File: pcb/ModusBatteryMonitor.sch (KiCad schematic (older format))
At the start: 17 parts, among them IC101 ATTINY3224-SS, IC102 MAX485/3485, P101 RS485, P102 NTC1, P103 NTC2, P104 DEBUG, P105 SHUNT+, P106 SHUNT-, P107 BAT-, U101 NCP1117ST50T3G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

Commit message: Made housing
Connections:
- net RS485-A: now also IC102.6 (A); no longer IC102.7 (B)
- net RS485-B: now also IC102.7 (B); no longer IC102.6 (A)
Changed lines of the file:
@@
 	1    0    0    -1
 $EndComp
+Text GLabel 9700 3650 2    60   BiDi ~ 0
+RS485-A
 Text GLabel 9700 3450 2    60   BiDi ~ 0
-RS485-A
-Text GLabel 9700 3650 2    60   BiDi ~ 0
 RS485-B
 $Comp

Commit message: Fixed NtC sensors and adjusted LUT
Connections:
- net RS485-A: now also P101.4; no longer P101.3
- net RS485-B: now also P101.3; no longer P101.4
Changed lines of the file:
@@
 	1    0    0    -1
 $EndComp
+Text GLabel 9500 4550 0    60   BiDi ~ 0
+RS485-A
 Text GLabel 9500 4450 0    60   BiDi ~ 0
-RS485-A
-Text GLabel 9500 4550 0    60   BiDi ~ 0
 RS485-B
 Text GLabel 9500 4350 0    60   BiDi ~ 0
@@
 	8500 5200 8500 5250
 $Comp
-L GND #PWR?
+L GND #PWR011
 U 1 1 63A05406
 P 9500 4650
-F 0 "#PWR?" H 9500 4650 30  0001 C CNN
+F 0 "#PWR011" H 9500 4650 30  0001 C CNN
 F 1 "GND" H 9500 4580 30  0001 C CNN
 F 2 "" H 9500 4650 60  0001 C CNN

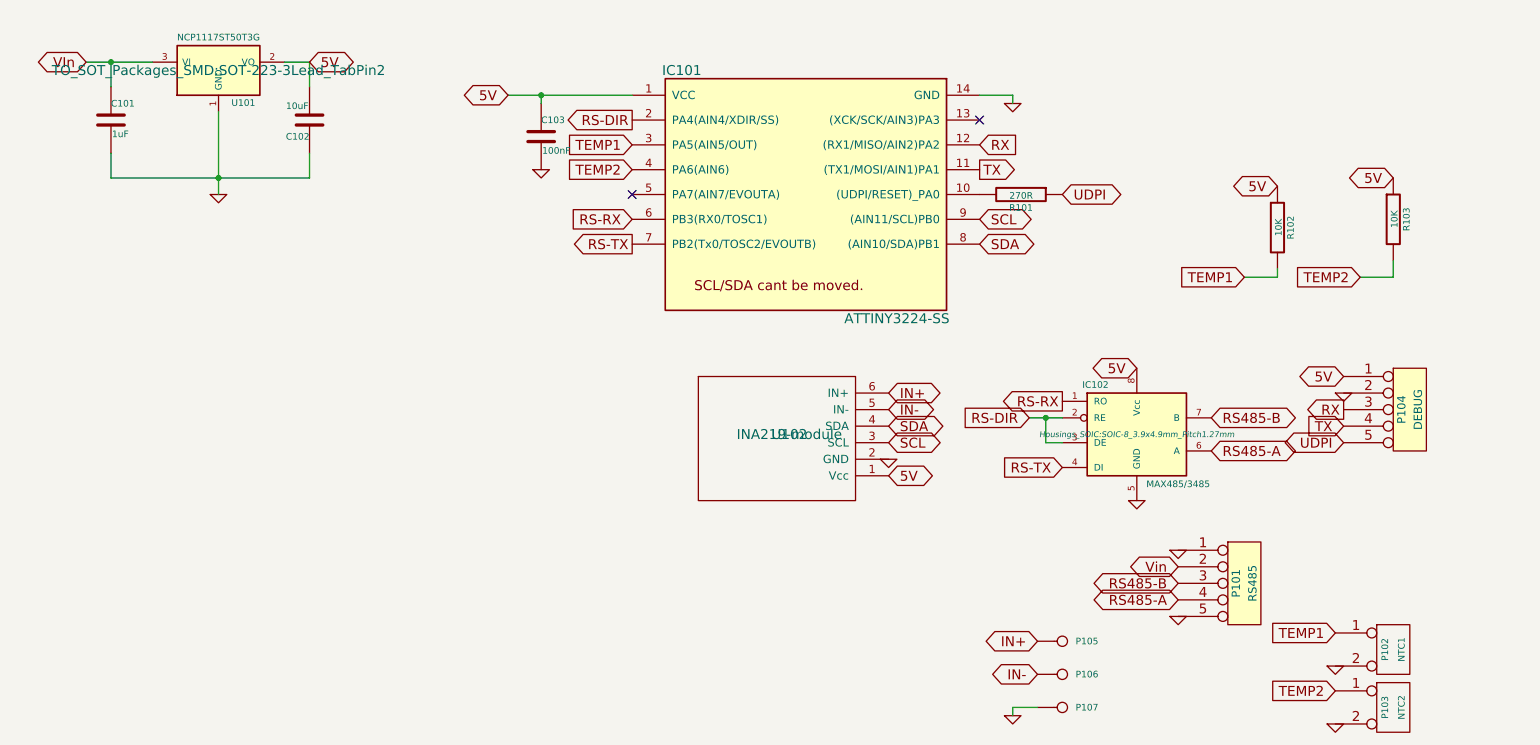
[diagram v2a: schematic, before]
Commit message: Added OLED display
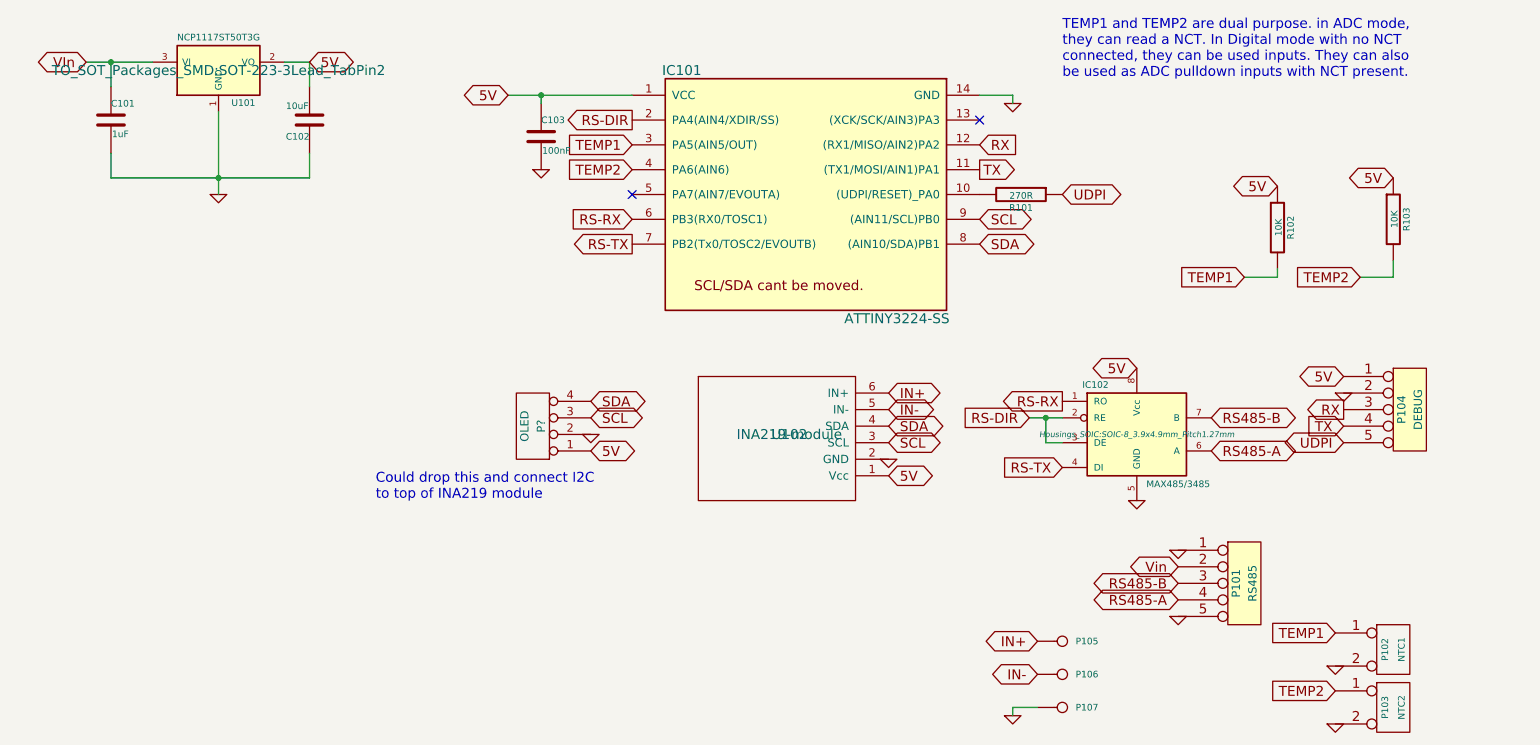
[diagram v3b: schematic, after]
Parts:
- added P?: OLED, symbol CONN_4
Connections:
- net 5V: now also P?.1 (P1)
- net GND: now also P?.2 (P2)
- net SCL: now also P?.3 (P3)
- net SDA: now also P?.4 (P4)
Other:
- note added: "Could drop this and connect I2C \nto top of INA219 module"
- note added: "TEMP1 and TEMP2 are dual purpose. in ADC mode, \nthey can read a NCT. In Digital mode with no NCT \nconnected, they can be used inputs. They can also \nbe used as ADC pulldown inputs with NCT present."
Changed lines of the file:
@@
 	1    0    0    -1
 $EndComp
+Text Notes 8800 1400 0    60   ~ 0
+TEMP1 and TEMP2 are dual purpose. in ADC mode, \nthey can read a NCT. In Digital mode with no NCT \nconnected, they can be used inputs. They can also \nbe used as ADC pulldown inputs with NCT present.
+$Comp
+L CONN_4 P?
+U 1 1 63C10AA1
+P 5600 3500
+F 0 "P?" V 5550 3500 50  0000 C CNN
+F 1 "OLED" V 5650 3500 50  0000 C CNN
+F 2 "" H 5600 3500 60  0001 C CNN
+F 3 "" H 5600 3500 60  0001 C CNN
+	1    5600 3500
+	-1   0    0    1
+$EndComp
+Text GLabel 5950 3650 2    60   BiDi ~ 0
+5V
+$Comp
+L GND #PWR?
+U 1 1 63C10B8E
+P 5950 3550
+F 0 "#PWR?" H 5950 3550 30  0001 C CNN
+F 1 "GND" H 5950 3480 30  0001 C CNN
+F 2 "" H 5950 3550 60  0001 C CNN
+F 3 "" H 5950 3550 60  0001 C CNN
+	1    5950 3550
+	1    0    0    -1
+$EndComp
+Text GLabel 5950 3450 2    60   BiDi ~ 0
+SCL
+Text GLabel 5950 3350 2    60   BiDi ~ 0
+SDA
+Text Notes 4650 3950 0    60   ~ 0
+Could drop this and connect I2C \nto top of INA219 module
 $EndSCHEMATC
